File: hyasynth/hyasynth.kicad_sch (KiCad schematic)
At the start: 28 parts, among them SW1 SW_SPST, SW10 G# Ab, SW11 A, SW12 A# Bb, SW13 B, SW14 C, SW15 Down Octave, SW16 Function, SW17 Up Octave, SW18 Reset, SW2 Low C, SW3 C# Db, SW4 D, SW5 D# Eb, SW6 E, SW7 F, SW8 F# Gb, SW9 G, U1 EFM8LB12F64E-B-QFN32

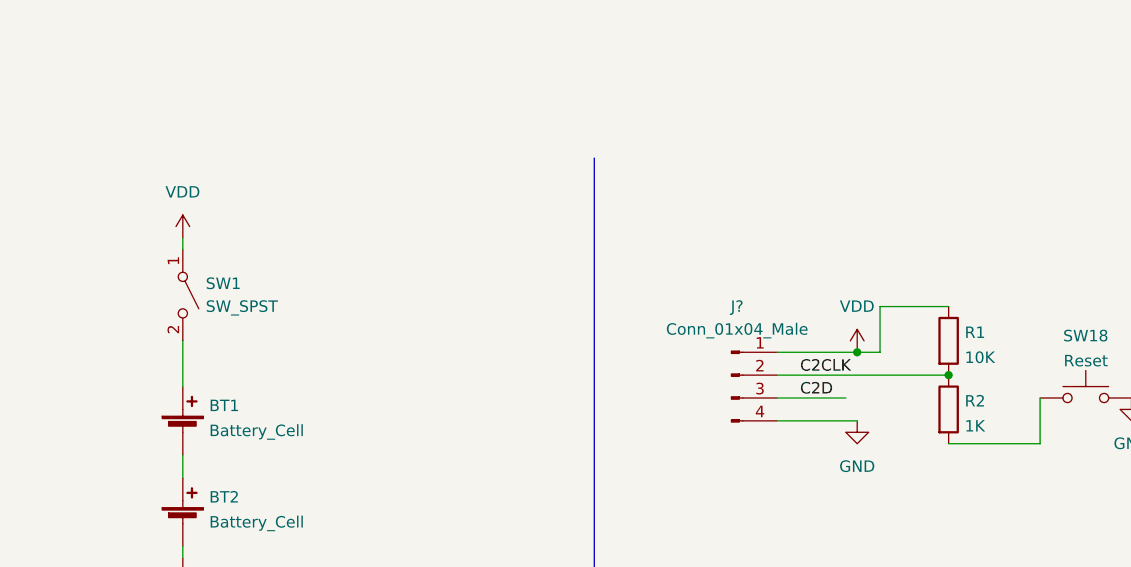
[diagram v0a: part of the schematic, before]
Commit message: Attached footprints to most things
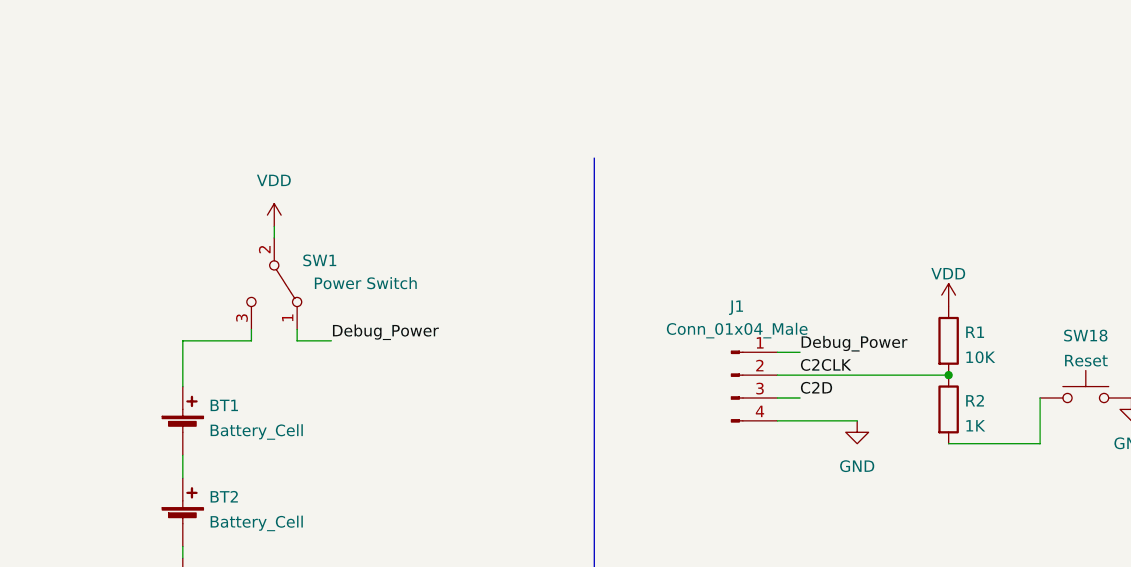
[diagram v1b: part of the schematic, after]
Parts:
- removed SW1: SW_SPST, symbol Switch:SW_SPST
- added SW1: Power Switch, symbol Switch:SW_SPDT
- BT1, BT2: footprint (none) -> Connector_PinSocket_2.54mm:PinSocket_1x02_P2.54mm_Vertical
- J1: renamed from J?; footprint (none) -> Connector_PinSocket_2.54mm:PinSocket_1x04_P2.54mm_Vertical
- SW10, SW11, SW12, SW13, SW14, SW15, SW16, SW17, SW18, SW2, SW3, SW4, SW5, SW6, SW7, SW8, SW9: footprint (none) -> Button_Switch_SMD:SW_Push_1P1T_NO_CK_KSC7xxJ
- U1: footprint QFN32_4X4_SIL -> QFN32:EFM8LB12F64E-B-QFN32
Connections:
- net VDD: now also SW1.2 (B); no longer J1.1 (Pin_1)
- net at BT1.1 (+): now also SW1.3 (C)
- new net Debug_Power: J1.1 (Pin_1), SW1.1 (A)

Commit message: Made changes to the schematic to fix bugs
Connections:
- net Keyboard Common is gone; now on net GND: SW10.1, SW11.1, SW12.1, SW13.1, SW14.1, SW2.1, SW3.1, SW4.1, SW5.1, SW6.1, SW7.1, SW8.1, SW9.1
- net C2CLK: no longer R1.2
- net GND: now also SW15.1, SW16.1, SW17.1
- net at R2.2, SW18.1: now also R1.2
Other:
- moved on the sheet: R1, R2, SW18
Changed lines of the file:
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@@
   (junction (at 69.85 185.42) (diameter 0) (color 0 0 0 0)
   )
+  (junction (at 267.97 158.75) (diameter 0) (color 0 0 0 0)
+  )
   (junction (at 215.9 64.77) (diameter 0) (color 0 0 0 0)
   )
@@
   (junction (at 181.61 36.83) (diameter 0) (color 0 0 0 0)
   )
+  (junction (at 123.19 36.83) (diameter 0) (color 0 0 0 0)
+  )
   (junction (at 36.83 175.26) (diameter 0) (color 0 0 0 0)
   )
@@
   (junction (at 36.83 185.42) (diameter 0) (color 0 0 0 0)
   )
-  (junction (at 116.84 36.83) (diameter 0) (color 0 0 0 0)
-  )
   (polyline (pts (xy 176.53 135.89) (xy 176.53 198.12))
     (stroke (width 0) (type default) (color 0 0 0 0))
@@
     (stroke (width 0) (type default) (color 0 0 0 0))
   )
+  (wire (pts (xy 119.38 36.83) (xy 123.19 36.83))
+    (stroke (width 0) (type default) (color 0 0 0 0))
+  )
   (wire (pts (xy 97.79 34.29) (xy 100.33 34.29))
     (stroke (width 0) (type default) (color 0 0 0 0))
@@
     (stroke (width 0) (type default) (color 0 0 0 0))
   )
-  (wire (pts (xy 116.84 44.45) (xy 127 44.45))
-    (stroke (width 0) (type default) (color 0 0 0 0))
-  )
   (wire (pts (xy 238.76 158.75) (xy 252.73 158.75))
     (stroke (width 0) (type default) (color 0 0 0 0))
@@
     (stroke (width 0) (type default) (color 0 0 0 0))
   )
+  (wire (pts (xy 97.79 36.83) (xy 111.76 36.83))
+    (stroke (width 0) (type default) (color 0 0 0 0))
+  )
   (wire (pts (xy 212.09 31.75) (xy 215.9 31.75))
     (stroke (width 0) (type default) (color 0 0 0 0))
@@
     (stroke (width 0) (type default) (color 0 0 0 0))
   )
-  (wire (pts (xy 127 44.45) (xy 127 39.37))
-    (stroke (width 0) (type default) (color 0 0 0 0))
-  )
   (wire (pts (xy 278.13 140.97) (xy 278.13 152.4))
     (stroke (width 0) (type default) (color 0 0 0 0))
@@
     (stroke (width 0) (type default) (color 0 0 0 0))
   )
+  (wire (pts (xy 267.97 158.75) (xy 270.51 158.75))
+    (stroke (width 0) (type default) (color 0 0 0 0))
+  )
   (wire (pts (xy 54.61 185.42) (xy 69.85 185.42))
     (stroke (width 0) (type default) (color 0 0 0 0))
   )
+  (wire (pts (xy 123.19 36.83) (xy 128.27 36.83))
+    (stroke (width 0) (type default) (color 0 0 0 0))
+  )
   (polyline (pts (xy 77.47 12.7) (xy 77.47 83.82))
     (stroke (width 0) (type default) (color 0 0 0 0))
@@
   )
   (wire (pts (xy 101.6 185.42) (xy 116.84 185.42))
-    (stroke (width 0) (type default) (color 0 0 0 0))
-  )
-  (wire (pts (xy 97.79 36.83) (xy 116.84 36.83))
     (stroke (width 0) (type default) (color 0 0 0 0))
   )
@@
     (effects (font (size 1.27 1.27)) (justify left bottom))
   )
+  (label "Cntl Common" (at 270.51 158.75 0)
+    (effects (font (size 1.27 1.27)) (justify left bottom))
+  )
   (label "A" (at 266.7 59.69 0)
     (effects (font (size 1.27 1.27)) (justify left bottom))
   )
-  (symbol (lib_id "Switch:SW_Push") (at 132.08 39.37 0) (unit 1)
-    (in_bom yes) (on_board yes) (fields_autoplaced)
-    (property "Reference" "SW18" (id 0) (at 132.08 32.4825 0))
-    (property "Value" "Reset" (id 1) (at 132.08 35.2576 0))
-    (property "Footprint" "Button_Switch_SMD:SW_Push_1P1T_NO_CK_KSC7xxJ" (id 2) (at 132.08 34.29 0)
-      (effects (font (size 1.27 1.27)) hide)
-    )
-    (property "Datasheet" "~" (id 3) (at 132.08 34.29 0)
+  (symbol (lib_id "Switch:SW_Push") (at 133.35 36.83 0) (unit 1)
+    (in_bom yes) (on_board yes) (fields_autoplaced)
+    (property "Reference" "SW18" (id 0) (at 133.35 29.9425 0))
+    (property "Value" "Reset" (id 1) (at 133.35 32.7176 0))
+    (property "Footprint" "Button_Switch_SMD:SW_Push_1P1T_NO_CK_KSC7xxJ" (id 2) (at 133.35 31.75 0)
+      (effects (font (size 1.27 1.27)) hide)
+    )
+    (property "Datasheet" "~" (id 3) (at 133.35 31.75 0)
       (effects (font (size 1.27 1.27)) hide)
     )
@@
     (pin "2")
   )
-  (symbol (lib_id "power:GND") (at 137.16 39.37 0) (unit 1)
-    (in_bom yes) (on_board yes) (fields_autoplaced)
-    (property "Reference" "#PWR0111" (id 0) (at 137.16 45.72 0)
-      (effects (font (size 1.27 1.27)) hide)
-    )
-    (property "Value" "GND" (id 1) (at 137.16 44.45 0))
-    (property "Footprint" "" (id 2) (at 137.16 39.37 0)
-      (effects (font (size 1.27 1.27)) hide)
-    )
-    (property "Datasheet" "" (id 3) (at 137.16 39.37 0)
+  (symbol (lib_id "power:GND") (at 138.43 36.83 0) (unit 1)
+    (in_bom yes) (on_board yes) (fields_autoplaced)
+    (property "Reference" "#PWR0111" (id 0) (at 138.43 43.18 0)
+      (effects (font (size 1.27 1.27)) hide)
+    )
+    (property "Value" "GND" (id 1) (at 138.43 41.91 0))
+    (property "Footprint" "" (id 2) (at 138.43 36.83 0)
+      (effects (font (size 1.27 1.27)) hide)
+    )
+    (property "Datasheet" "" (id 3) (at 138.43 36.83 0)
       (effects (font (size 1.27 1.27)) hide)
     )
@@
     (pin "1")
   )
-  (symbol (lib_id "Device:R") (at 116.84 40.64 0) (unit 1)
-    (in_bom yes) (on_board yes) (fields_autoplaced)
-    (property "Reference" "R2" (id 0) (at 118.618 39.7315 0)
-      (effects (font (size 1.27 1.27)) (justify left))
-    )
-    (property "Value" "1K" (id 1) (at 118.618 42.5066 0)
-      (effects (font (size 1.27 1.27)) (justify left))
-    )
-    (property "Footprint" "" (id 2) (at 115.062 40.64 90)
-      (effects (font (size 1.27 1.27)) hide)
-    )
-    (property "Datasheet" "~" (id 3) (at 116.84 40.64 0)
+  (symbol (lib_id "Device:R") (at 115.57 36.83 90) (unit 1)
+    (in_bom yes) (on_board yes) (fields_autoplaced)
+    (property "Reference" "R2" (id 0) (at 115.57 31.8475 90))
+    (property "Value" "1K" (id 1) (at 115.57 34.6226 90))
+    (property "Footprint" "" (id 2) (at 115.57 38.608 90)
+      (effects (font (size 1.27 1.27)) hide)
+    )
+    (property "Datasheet" "~" (id 3) (at 115.57 36.83 0)
       (effects (font (size 1.27 1.27)) hide)
     )
@@
     (pin "1")
     (pin "2")
+  )
+  (symbol (lib_id "power:GND") (at 270.51 158.75 0) (unit 1)
+    (in_bom yes) (on_board yes) (fields_autoplaced)
+    (property "Reference" "#PWR?" (id 0) (at 270.51 165.1 0)
+      (effects (font (size 1.27 1.27)) hide)
+    )
+    (property "Value" "GND" (id 1) (at 270.51 163.3125 0))
+    (property "Footprint" "" (id 2) (at 270.51 158.75 0)
+      (effects (font (size 1.27 1.27)) hide)
+    )
+    (property "Datasheet" "" (id 3) (at 270.51 158.75 0)
+      (effects (font (size 1.27 1.27)) hide)
+    )
+    (pin "1")
   )
   (symbol (lib_id "Switch:SW_Push") (at 74.93 175.26 0) (unit 1)
@@
     (pin "2")
   )
+  (symbol (lib_id "power:GND") (at 151.13 185.42 0) (unit 1)
+    (in_bom yes) (on_board yes) (fields_autoplaced)
+    (property "Reference" "#PWR?" (id 0) (at 151.13 191.77 0)
+      (effects (font (size 1.27 1.27)) hide)
+    )
+    (property "Value" "GND" (id 1) (at 151.13 189.9825 0))
+    (property "Footprint" "" (id 2) (at 151.13 185.42 0)
+      (effects (font (size 1.27 1.27)) hide)
+    )
+    (property "Datasheet" "" (id 3) (at 151.13 185.42 0)
+      (effects (font (size 1.27 1.27)) hide)
+    )
+    (pin "1")
+  )
   (symbol (lib_id "power:GND") (at 208.28 50.8 0) (unit 1)
     (in_bom yes) (on_board yes) (fields_autoplaced)
@@
     (pin "1")
   )
-  (symbol (lib_id "power:VDD") (at 116.84 29.21 0) (unit 1)
-    (in_bom yes) (on_board yes) (fields_autoplaced)
-    (property "Reference" "#PWR0110" (id 0) (at 116.84 33.02 0)
-      (effects (font (size 1.27 1.27)) hide)
-    )
-    (property "Value" "VDD" (id 1) (at 116.84 25.6055 0))
-    (property "Footprint" "" (id 2) (at 116.84 29.21 0)
-      (effects (font (size 1.27 1.27)) hide)
-    )
-    (property "Datasheet" "" (id 3) (at 116.84 29.21 0)
-      (effects (font (size 1.27 1.27)) hide)
-    )
-    (pin "1")
-  )
-  (symbol (lib_id "Device:R") (at 116.84 33.02 0) (unit 1)
-    (in_bom yes) (on_board yes) (fields_autoplaced)
-    (property "Reference" "R1" (id 0) (at 118.618 32.1115 0)
-      (effects (font (size 1.27 1.27)) (justify left))
-    )
-    (property "Value" "10K" (id 1) (at 118.618 34.8866 0)
-      (effects (font (size 1.27 1.27)) (justify left))
-    )
-    (property "Footprint" "" (id 2) (at 115.062 33.02 90)
-      (effects (font (size 1.27 1.27)) hide)
-    )
-    (property "Datasheet" "~" (id 3) (at 116.84 33.02 0)
+  (symbol (lib_id "power:VDD") (at 123.19 29.21 0) (unit 1)
+    (in_bom yes) (on_board yes) (fields_autoplaced)
+    (property "Reference" "#PWR0110" (id 0) (at 123.19 33.02 0)
+      (effects (font (size 1.27 1.27)) hide)
+    )
+    (property "Value" "VDD" (id 1) (at 123.19 25.6055 0))
+    (property "Footprint" "" (id 2) (at 123.19 29.21 0)
+      (effects (font (size 1.27 1.27)) hide)
+    )
+    (property "Datasheet" "" (id 3) (at 123.19 29.21 0)
+      (effects (font (size 1.27 1.27)) hide)
+    )
+    (pin "1")
+  )
+  (symbol (lib_id "Device:R") (at 123.19 33.02 0) (unit 1)
+    (in_bom yes) (on_board yes) (fields_autoplaced)
+    (property "Reference" "R1" (id 0) (at 124.968 32.1115 0)
+      (effects (font (size 1.27 1.27)) (justify left))
+    )
+    (property "Value" "10K" (id 1) (at 124.968 34.8866 0)
+      (effects (font (size 1.27 1.27)) (justify left))
+    )
+    (property "Footprint" "" (id 2) (at 121.412 33.02 90)
+      (effects (font (size 1.27 1.27)) hide)
+    )
+    (property "Datasheet" "~" (id 3) (at 123.19 33.02 0)
       (effects (font (size 1.27 1.27)) hide)
     )
@@
       (reference "#PWR0113") (unit 1) (value "VDD") (footprint "")
     )
+    (path "/8588d019-3df7-4e6c-99b4-c25e560e198f"
+      (reference "#PWR?") (unit 1) (value "GND") (footprint "")
+    )
+    (path "/b6c57aeb-0997-46a3-9323-1afc6e631db8"
+      (reference "#PWR?") (unit 1) (value "GND") (footprint "")
+    )
     (path "/1b998674-f60c-49d7-94e3-7408ec140148"

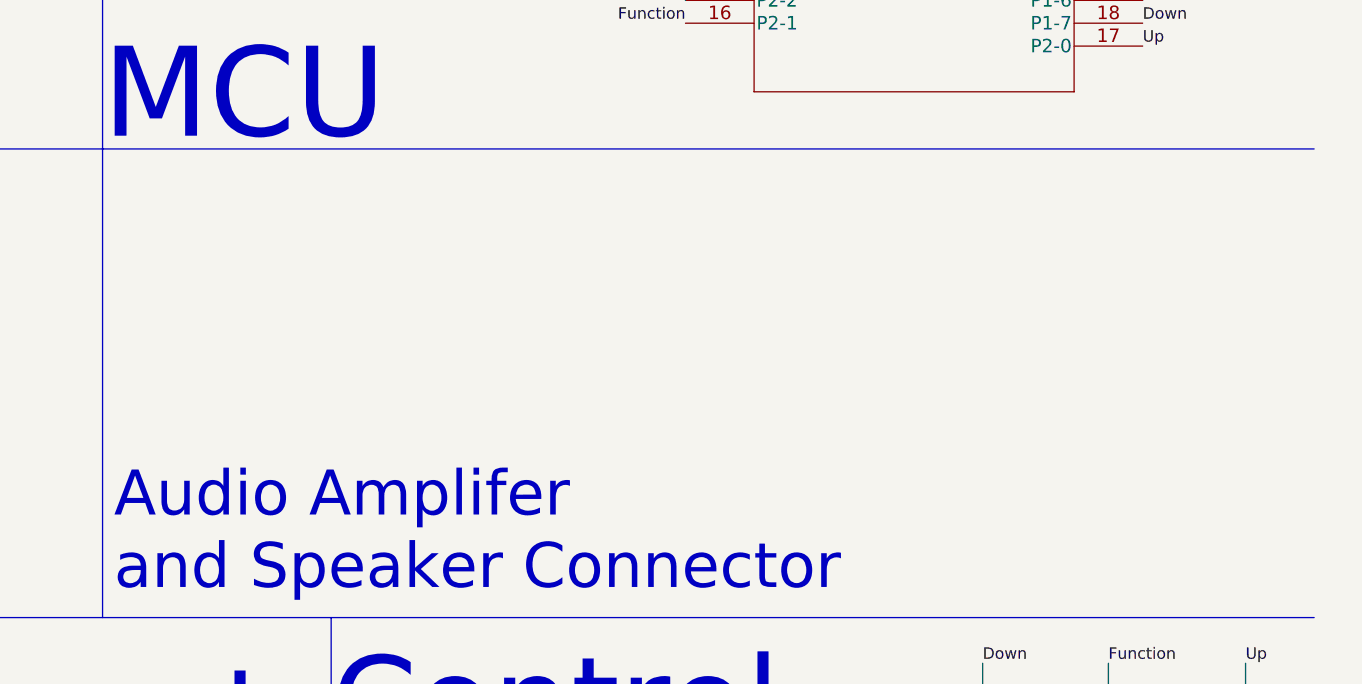
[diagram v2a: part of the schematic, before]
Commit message: Power Amplifier for speaker output
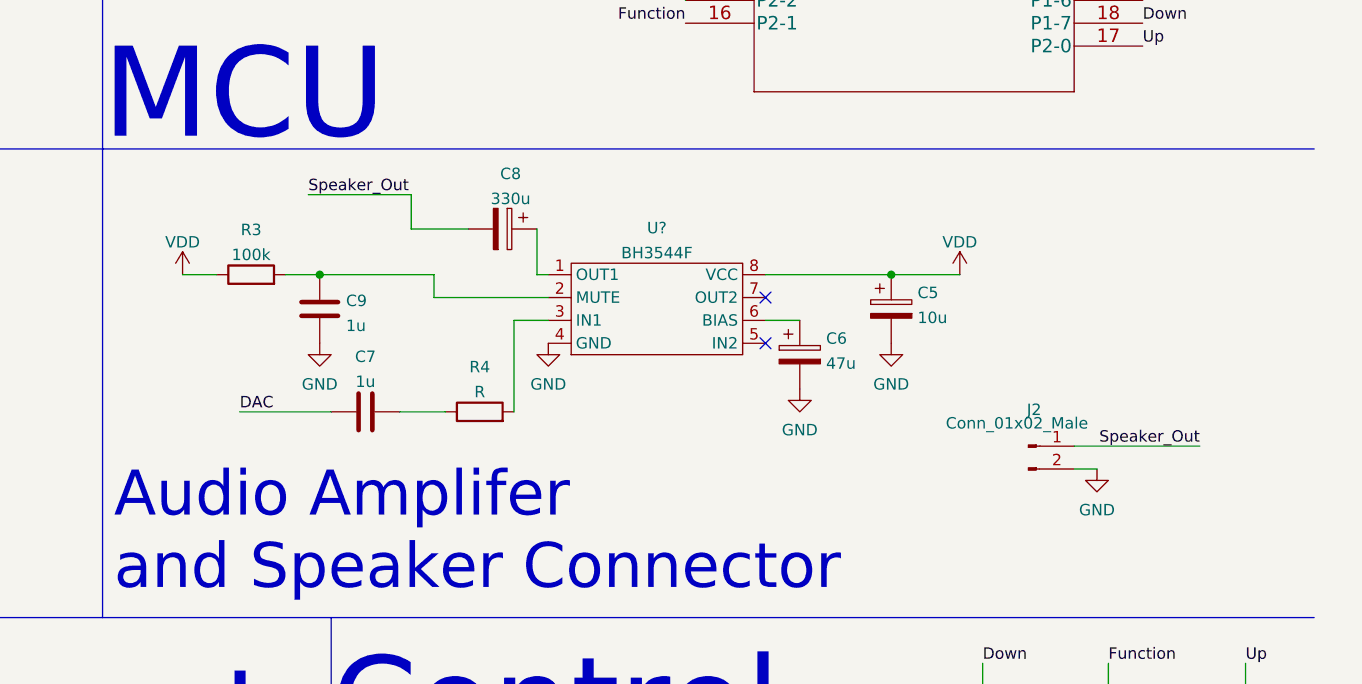
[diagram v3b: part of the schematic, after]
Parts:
- added C5: 10u, symbol Device:C_Polarized
- added C6: 47u, symbol Device:C_Polarized
- added C7, C9: 1u, symbol Device:C
- added C8: 330u, symbol Device:C_Polarized
- added J2: Conn_01x02_Male, symbol Connector:Conn_01x02_Male
- added R3: 100k, symbol Device:R
- added R4: R, symbol Device:R
- added U?: BH3544F, symbol BH3544F:BH3544F
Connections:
- net DAC: now also C7.1
- net GND: now also C5.2, C6.2, C9.2, J2.2 (Pin_2), U?.4 (GND)
- net VDD: now also C5.1, R3.1, U?.8 (VCC)
- new net: C9.1, R3.2, U?.2 (MUTE)
- new net: C6.1, U?.6 (BIAS)
- new net: C7.2, R4.1
- new net: R4.2, U?.3 (IN1)
- new net: C8.1, U?.1 (OUT1)
- new net Speaker_Out: C8.2, J2.1 (Pin_1)
- no-connect marks 0 -> 2

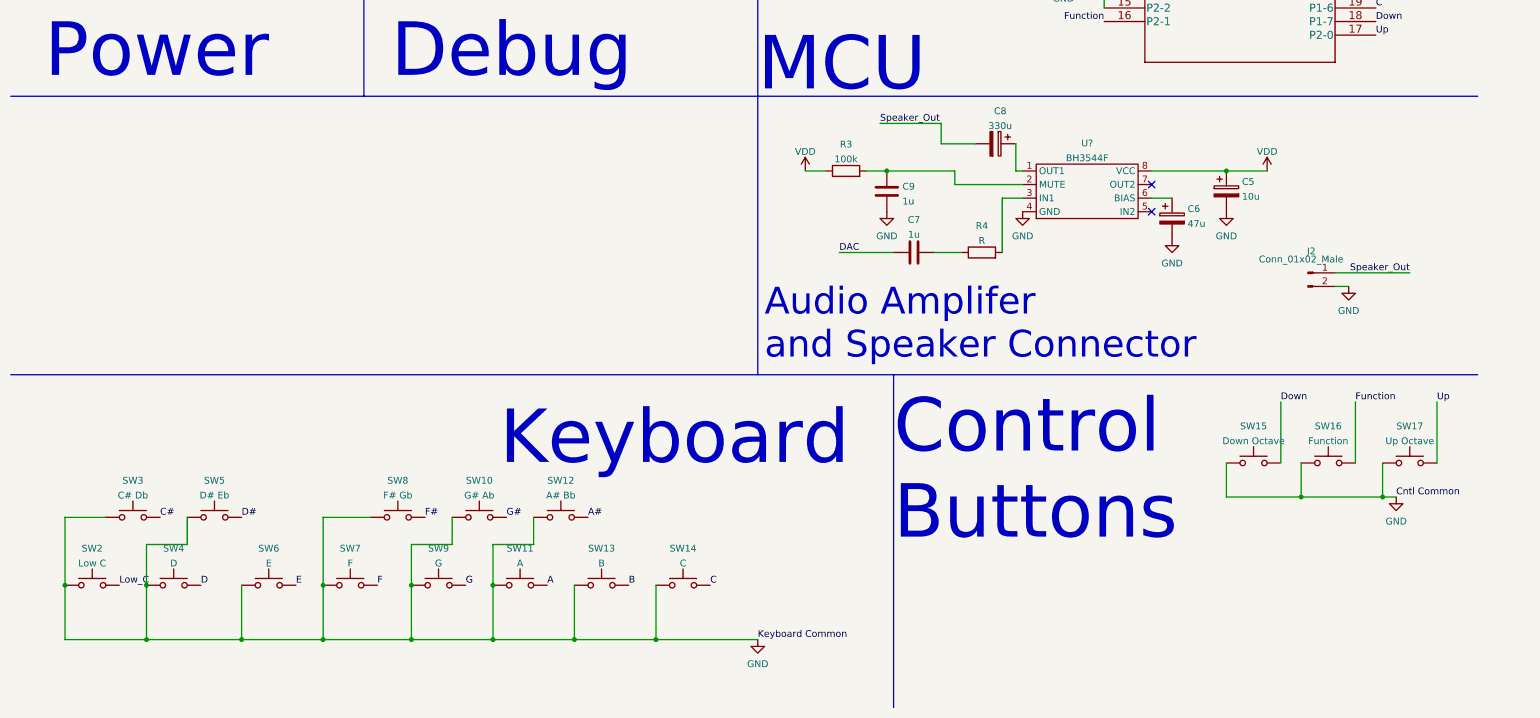
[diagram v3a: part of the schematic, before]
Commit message: Added a jumper
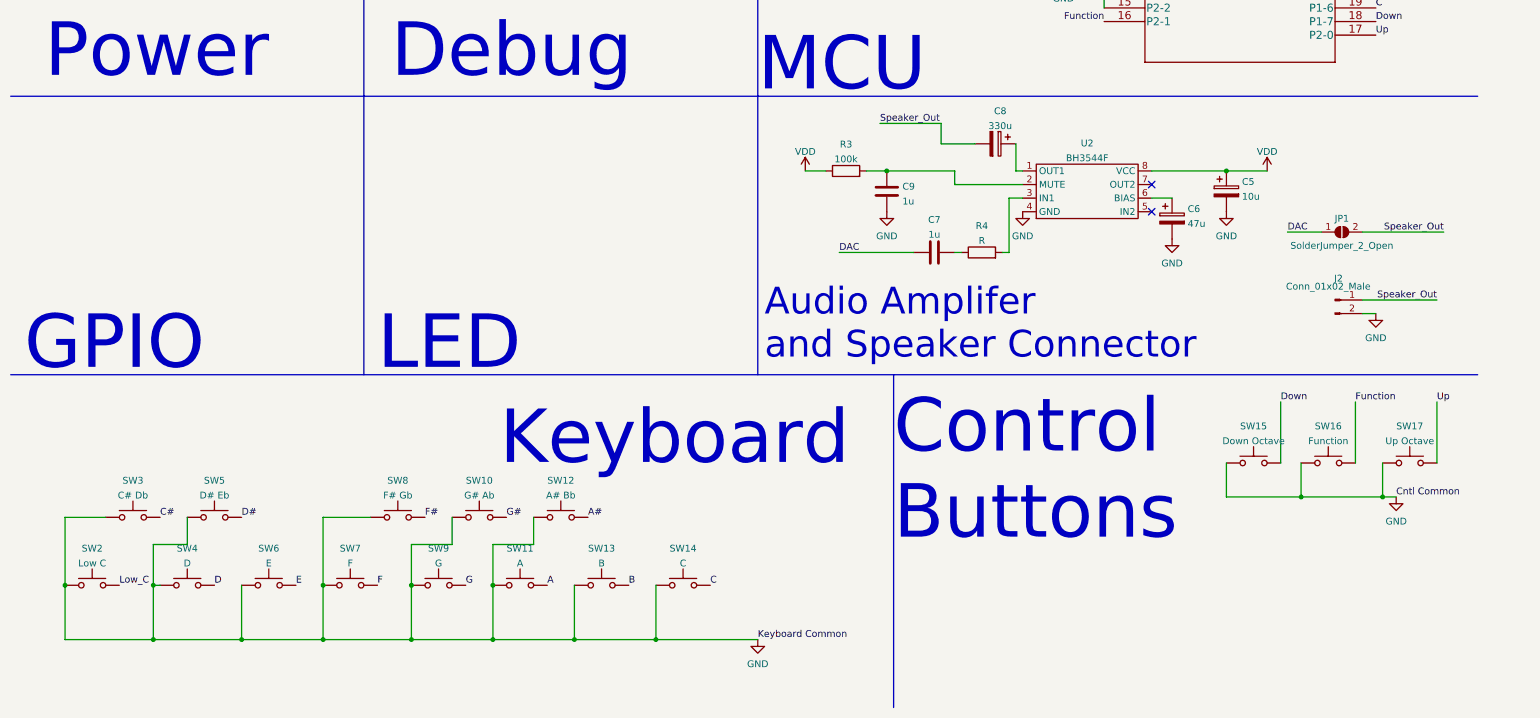
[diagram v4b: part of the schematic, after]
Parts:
- added JP1: SolderJumper_2_Open, symbol Jumper:SolderJumper_2_Open
- gave numbers to parts that had none: 1
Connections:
- net DAC: now also JP1.1 (A)
- net Speaker_Out: now also JP1.2 (B)
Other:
- note added: "GPIO"
- note added: "LED"
- moved on the sheet: C7, J2, SW4
